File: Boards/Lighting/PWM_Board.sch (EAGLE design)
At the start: 54 parts, among them Q1 N-FET, Q10 N-FET, Q11 N-FET, Q12 N-FET, Q13 N-FET, Q14 N-FET, Q15 N-FET, Q16 N-FET, Q17 N-FET, Q18 N-FET, Q19 N-FET, Q2 N-FET, Q20 N-FET, Q21 N-FET, Q22 N-FET, Q23 N-FET, Q24 N-FET, Q25 N-FET, Q26 N-FET, Q27 N-FET, Q28 N-FET, Q29 N-FET, Q3 N-FET, Q30 N-FET, Q31 N-FET, Q32 N-FET, Q4 N-FET, Q5 N-FET, Q6 N-FET, Q7 N-FET, Q8 N-FET, Q9 N-FET

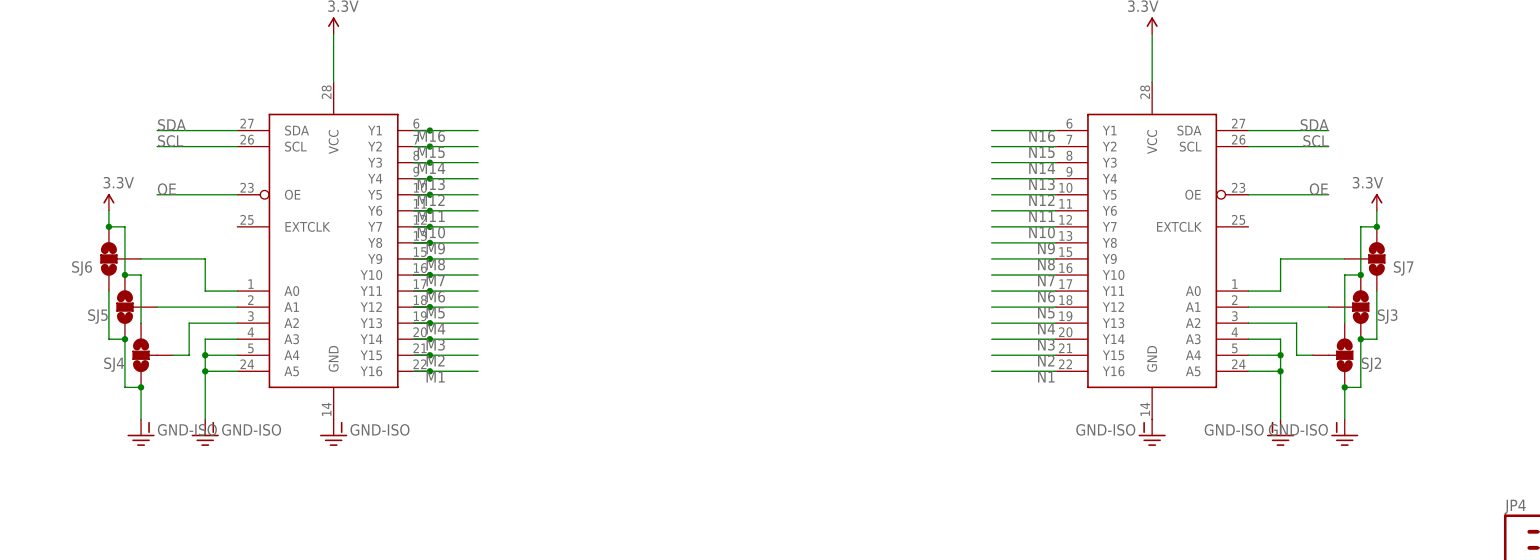
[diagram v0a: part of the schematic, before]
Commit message: Finished PWM lighting board, now uses a ribbon cable to connect to a break out terminal board
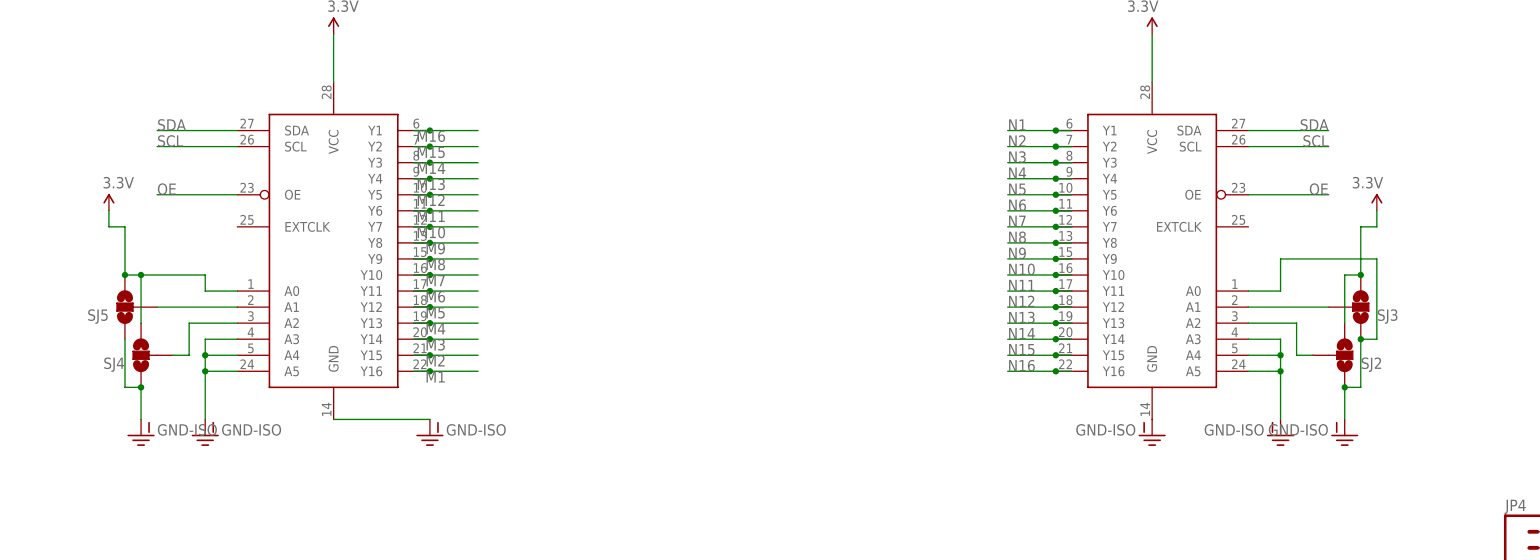
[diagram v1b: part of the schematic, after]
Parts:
- removed SJ6, SJ7: (no value), 1_SparkFun-Passives:SOLDERJUMPER_2WAYS
- renumbered U$1 to U$2
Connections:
- removed net N$43: SJ7.2, U$2.A0
- removed net N$46: SJ6.2, U$3.A0
- net 3.3V: now also U$3.A0; no longer SJ6.3, SJ7.3
- net GND-ISO: now also U$2.A0; no longer SJ6.1, SJ7.1
- net N1: now also U$2.Y1; no longer U$2.Y16
- net N10: now also U$2.Y10; no longer U$2.Y7
- net N11: now also U$2.Y11; no longer U$2.Y6
- net N12: now also U$2.Y12; no longer U$2.Y5
- net N13: now also U$2.Y13; no longer U$2.Y4
- net N14: now also U$2.Y14; no longer U$2.Y3
- net N15: now also U$2.Y15; no longer U$2.Y2
- net N16: now also U$2.Y16; no longer U$2.Y1
- net N2: now also U$2.Y2; no longer U$2.Y15
- net N3: now also U$2.Y3; no longer U$2.Y14
- net N4: now also U$2.Y4; no longer U$2.Y13
- net N5: now also U$2.Y5; no longer U$2.Y12
- net N6: now also U$2.Y6; no longer U$2.Y11
- net N7: now also U$2.Y7; no longer U$2.Y10
- net N8: now also U$2.Y8; no longer U$2.Y9
- net N9: now also U$2.Y9; no longer U$2.Y8
